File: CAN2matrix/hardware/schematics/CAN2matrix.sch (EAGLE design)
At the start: 20 parts, among them IC1 MEGA8-P, IC2 MCP2515-E/P, IC3 MCP2515-E/P, U1 MCP2551P, U2 MCP2551P, X1 CAN1, X2 CAN2

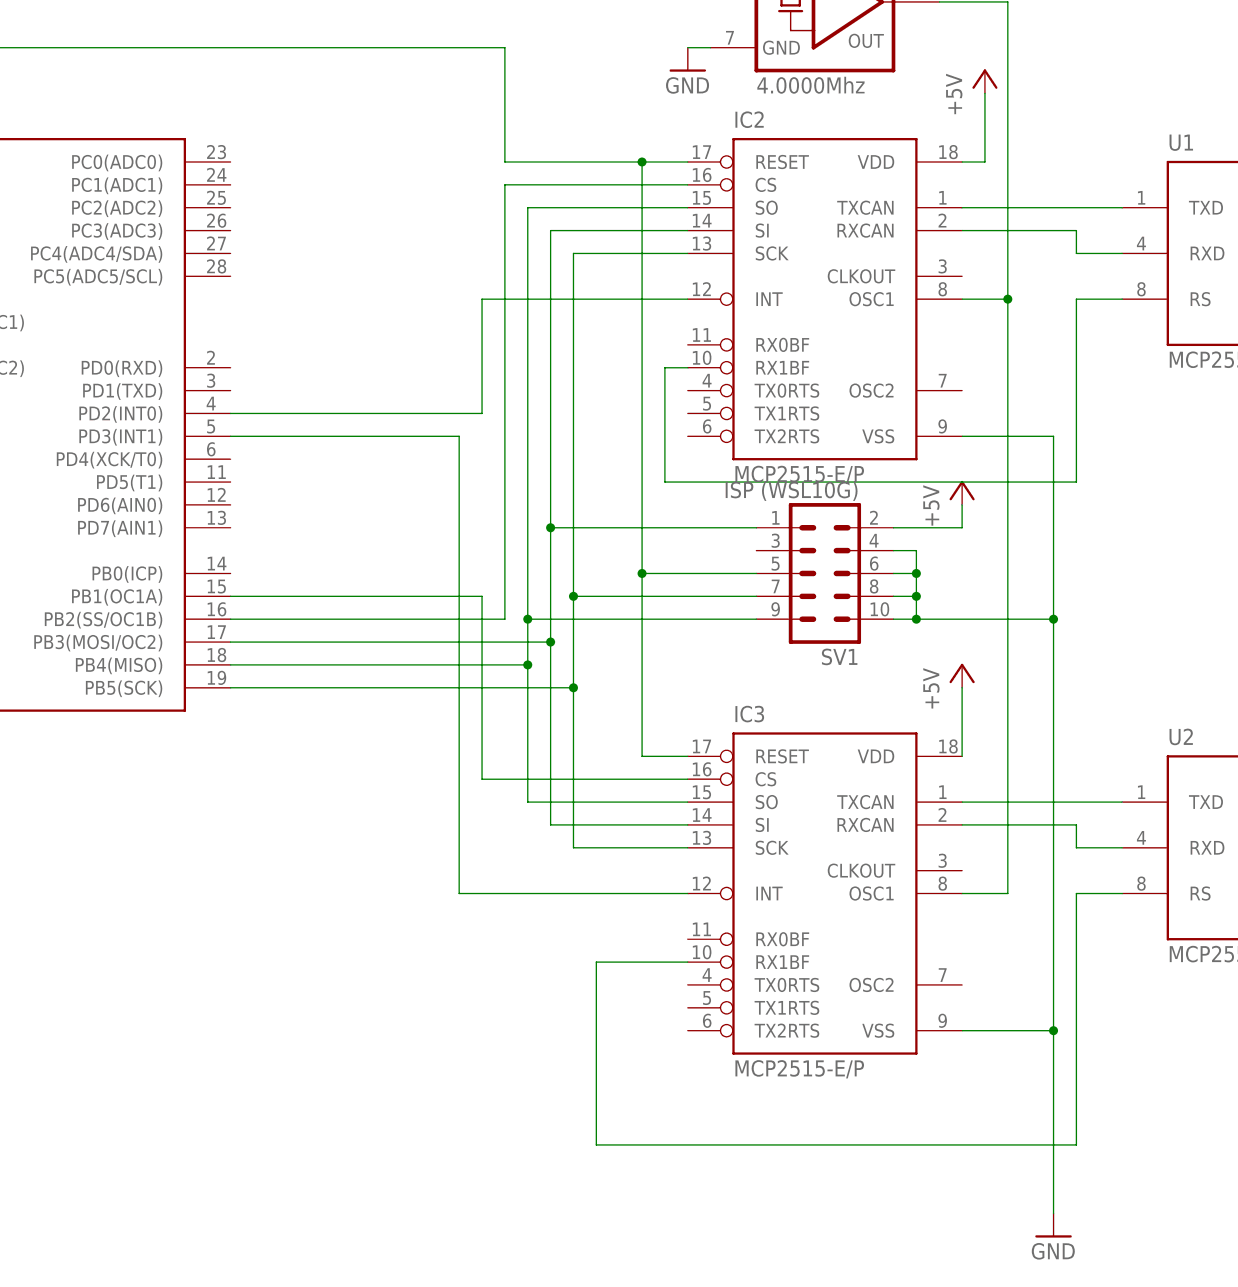
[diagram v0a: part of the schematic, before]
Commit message: update schematics to provide possibility to disconnect ISP power supply from board
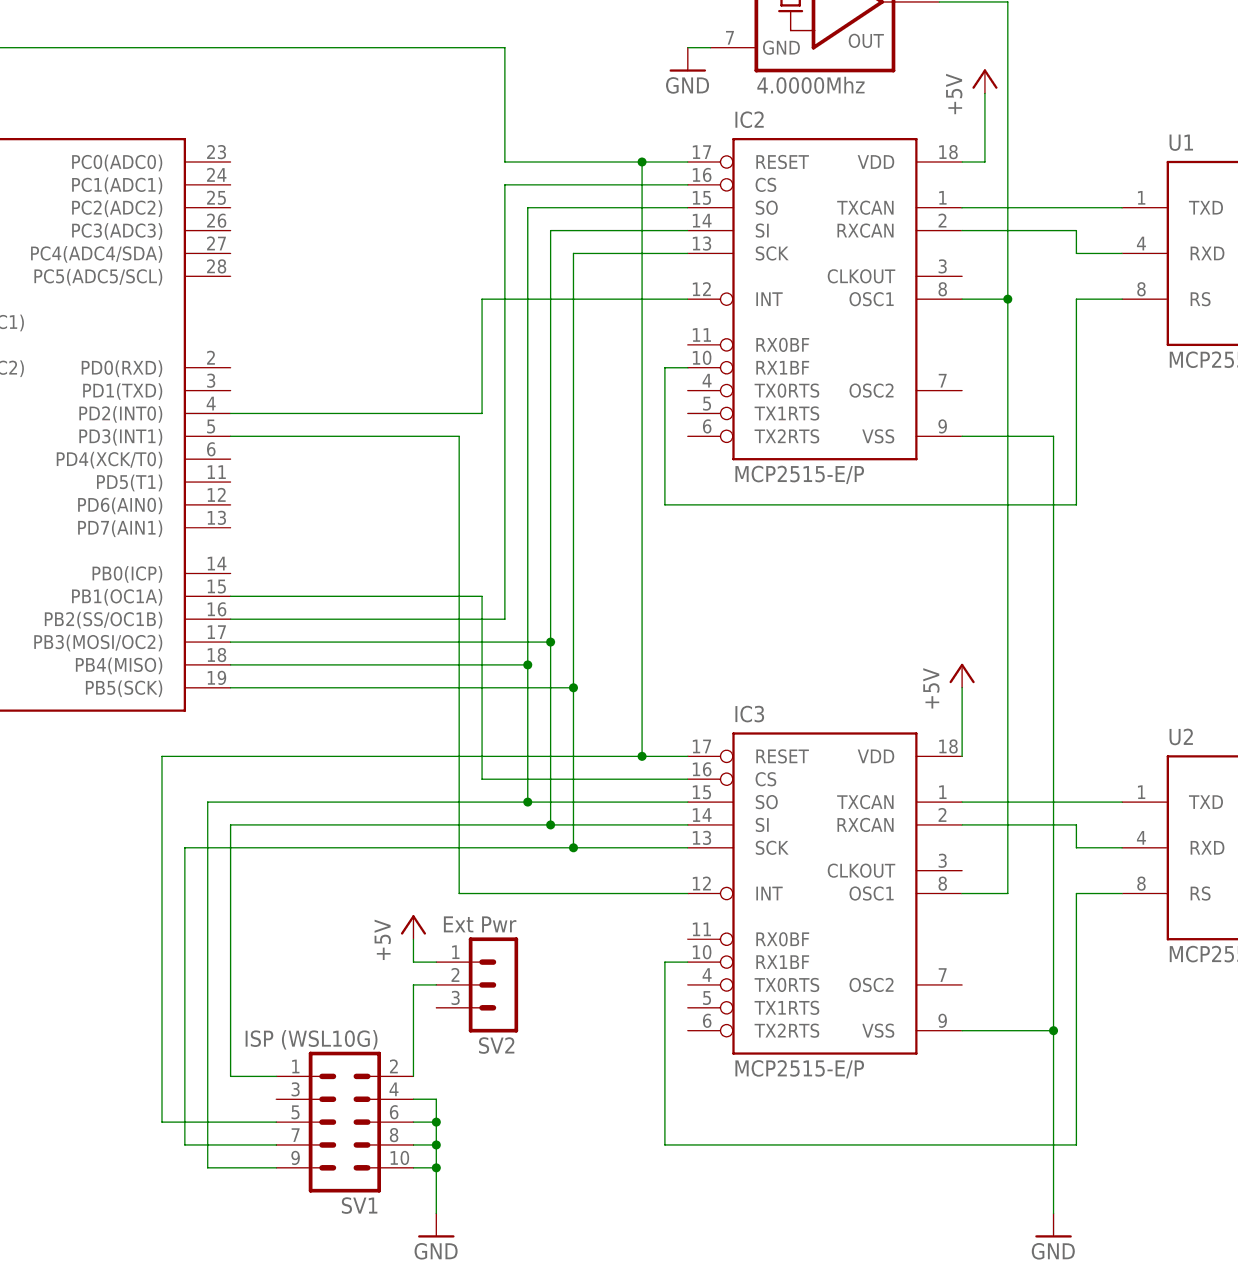
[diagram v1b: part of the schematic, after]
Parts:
- added SV2: Ext Pwr, con-lstb:MA03-1
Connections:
- new net N$21: SV1.2, SV2.2
- net +5V: now also SV2.1; no longer SV1.2
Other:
- moved on the sheet: SV1

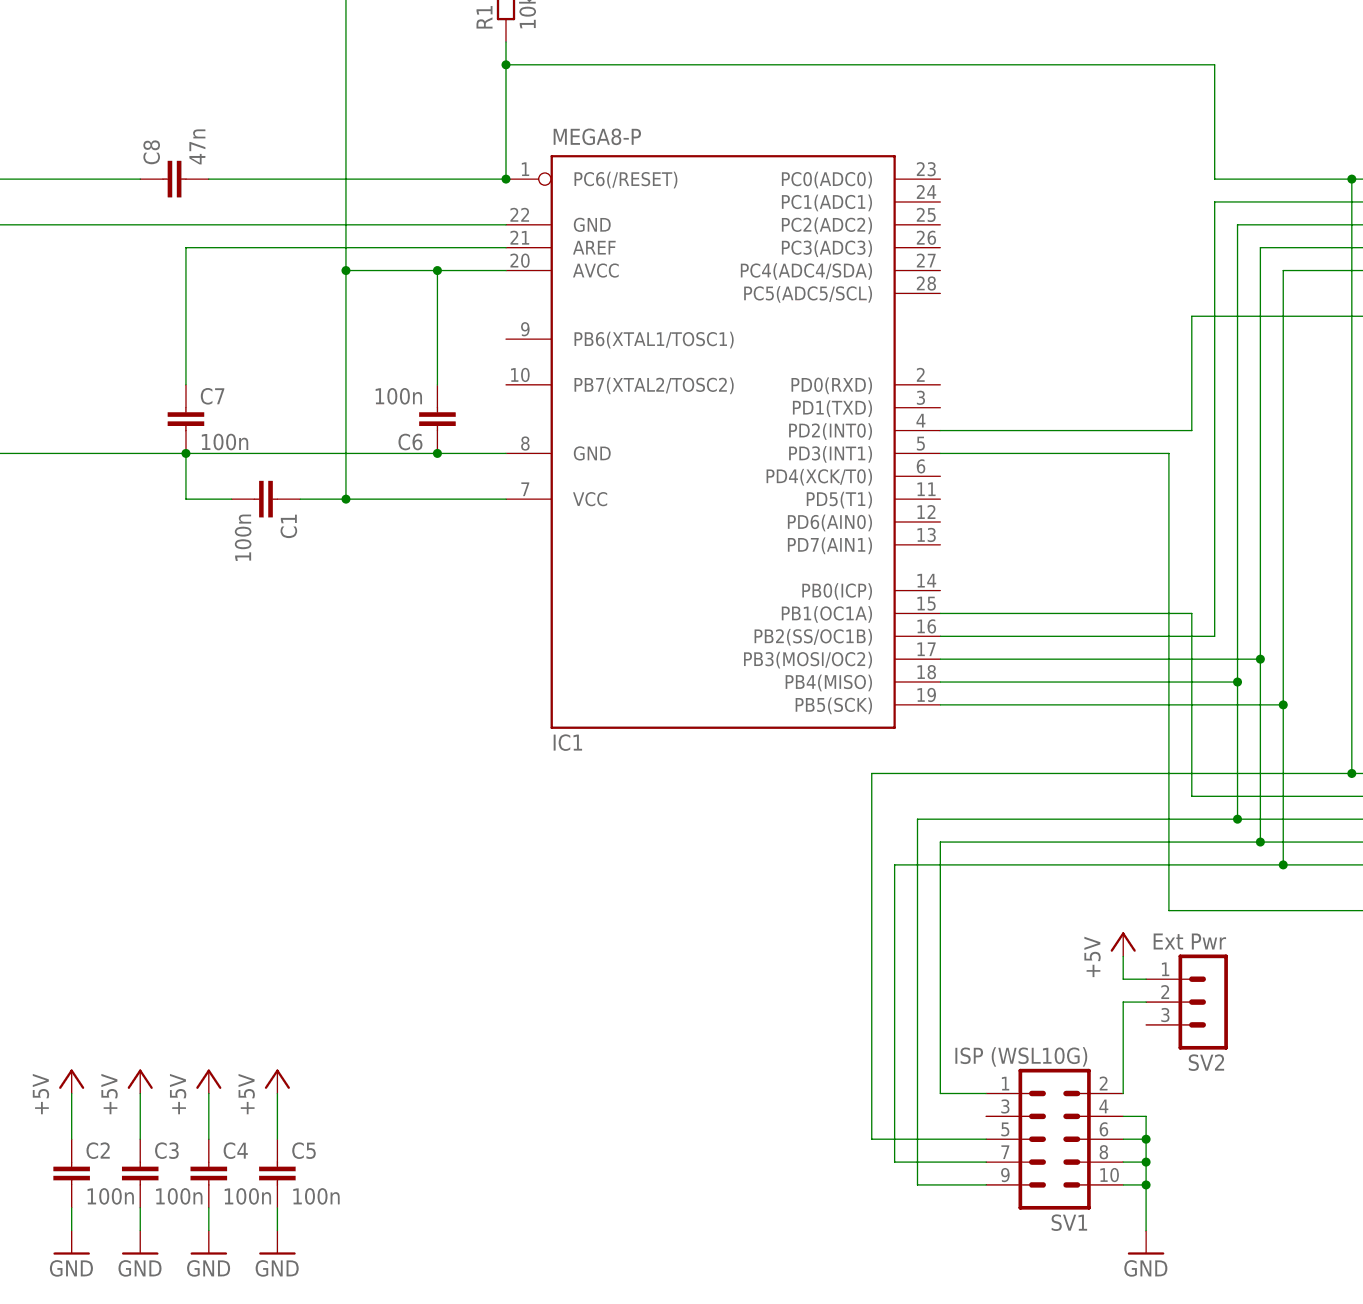
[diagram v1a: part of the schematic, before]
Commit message: add LEDs to schematics
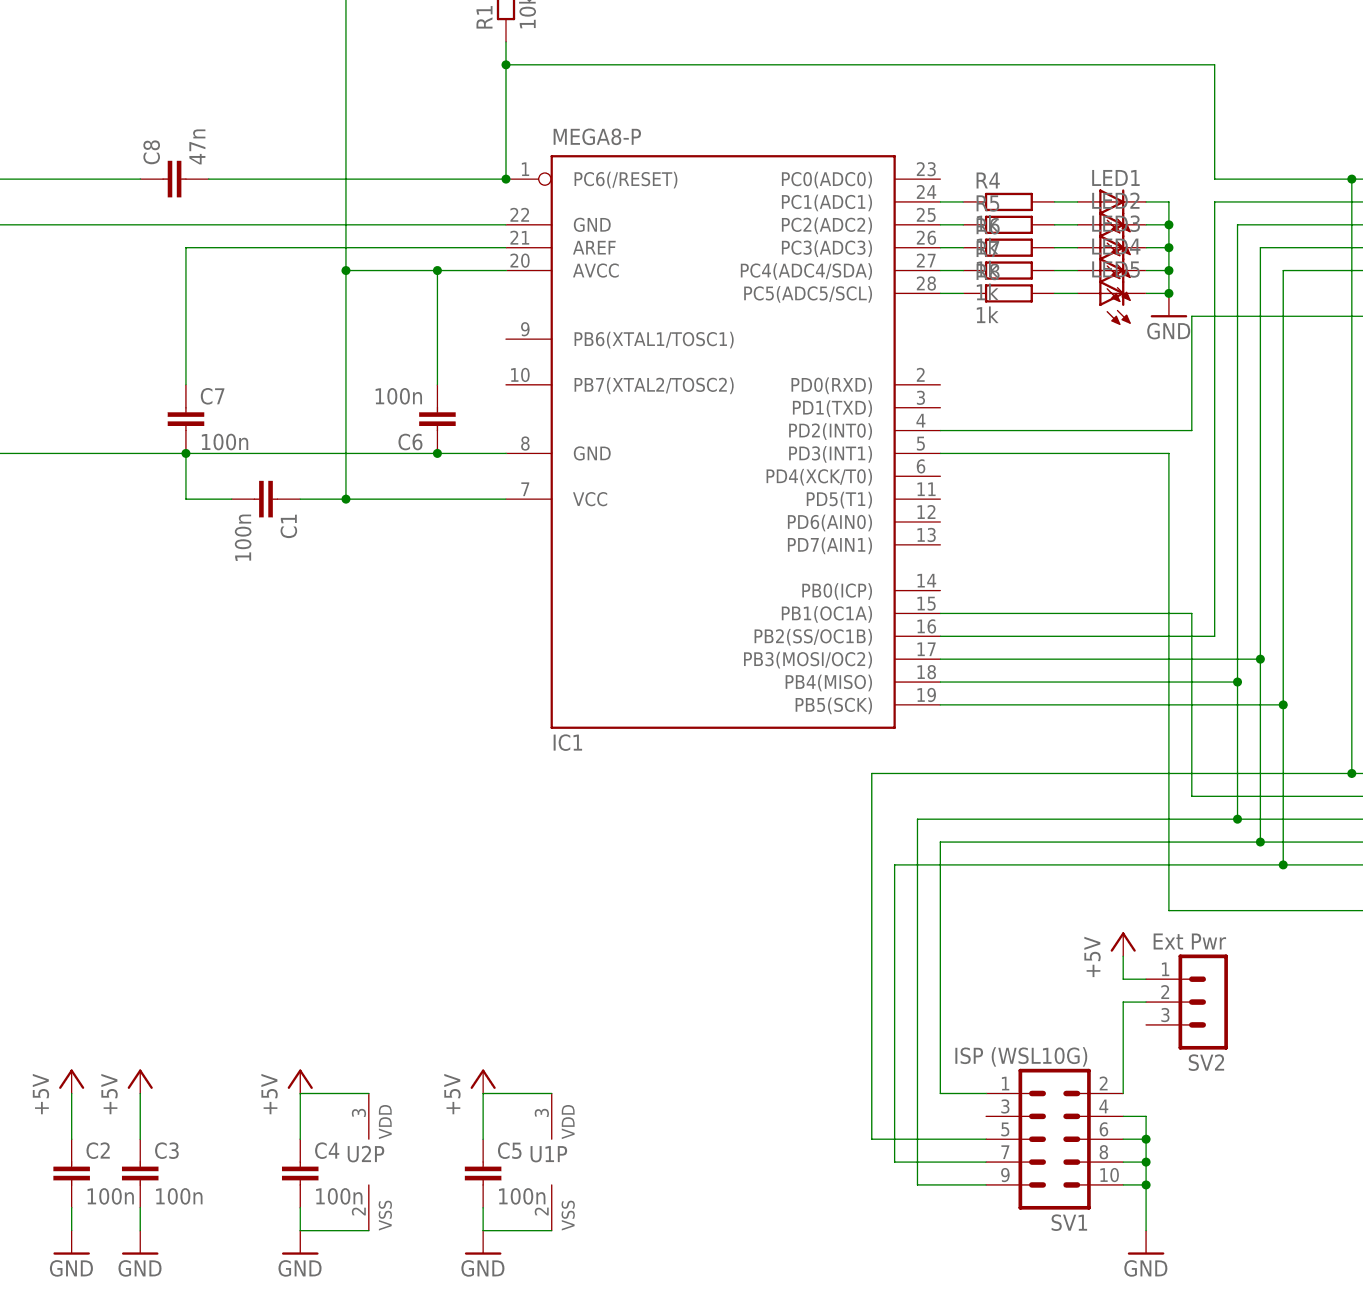
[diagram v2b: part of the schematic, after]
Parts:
- added LED1, LED2, LED3, LED4, LED5: (no value), led:LED3MM
- added R4, R5, R6, R7, R8: 1k, resistor:R-EU_0207/2V
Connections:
- new net N$22: IC1.PC1(ADC1), R4.1
- new net N$23: IC1.PC2(ADC2), R5.1
- new net N$24: IC1.PC3(ADC3), R6.1
- new net N$25: IC1.PC4(ADC4/SDA), R7.1
- new net N$26: IC1.PC5(ADC5/SCL), R8.1
- new net N$27: LED1.A, R4.2
- new net N$28: LED2.A, R5.2
- new net N$29: LED3.A, R6.2
- new net N$30: LED4.A, R7.2
- new net N$31: LED5.A, R8.2
- net +5V: now also U1P.VDD, U2P.VDD
- net GND: now also LED1.C, LED2.C, LED3.C, LED4.C, LED5.C, U1P.VSS, U2P.VSS
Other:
- moved on the sheet: C4, C5
